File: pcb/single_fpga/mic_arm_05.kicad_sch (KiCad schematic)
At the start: 18 parts, among them U104 CDCLVC1108PW, U41 IM72D128V01XTMA1, U42 IM72D128V01XTMA1, U43 IM72D128V01XTMA1, U44 IM72D128V01XTMA1, U45 IM72D128V01XTMA1, U46 IM72D128V01XTMA1, U47 IM72D128V01XTMA1, U48 IM72D128V01XTMA1

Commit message: Fixed symbol library references.
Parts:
- U104: footprint PW0016A_N -> CDCLVC1108:PW0016A_N
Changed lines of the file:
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@@
 			)
 		)
-		(property "Footprint" "PW0016A_N"
+		(property "Footprint" "CDCLVC1108:PW0016A_N"
 			(at 229.87 95.25 0)
 			(hide yes)

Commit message: Fixed footprints. Added missing mic. Relinked placed footprints.
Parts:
- U41, U42, U43, U44, U45, U46, U47, U48: footprint (none) -> IM72D128:IFX-PG-LLGA-5-4
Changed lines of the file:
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@@
 			)
 		)
-		(property "Footprint" ""
+		(property "Footprint" "IM72D128:IFX-PG-LLGA-5-4"
 			(at 59.69 160.02 0)
 			(hide yes)
@@
 			)
 		)
-		(property "Footprint" ""
+		(property "Footprint" "IM72D128:IFX-PG-LLGA-5-4"
 			(at 135.89 160.02 0)
 			(hide yes)
@@
 			)
 		)
-		(property "Footprint" ""
+		(property "Footprint" "IM72D128:IFX-PG-LLGA-5-4"
 			(at 59.69 83.82 0)
 			(hide yes)
@@
 			)
 		)
-		(property "Footprint" ""
+		(property "Footprint" "IM72D128:IFX-PG-LLGA-5-4"
 			(at 59.69 120.65 0)
 			(hide yes)
@@
 			)
 		)
-		(property "Footprint" ""
+		(property "Footprint" "IM72D128:IFX-PG-LLGA-5-4"
 			(at 59.69 44.45 0)
 			(hide yes)
@@
 			)
 		)
-		(property "Footprint" ""
+		(property "Footprint" "IM72D128:IFX-PG-LLGA-5-4"
 			(at 135.89 83.82 0)
 			(hide yes)
@@
 			)
 		)
-		(property "Footprint" ""
+		(property "Footprint" "IM72D128:IFX-PG-LLGA-5-4"
 			(at 135.89 44.45 0)
 			(hide yes)
@@
 			)
 		)
-		(property "Footprint" ""
+		(property "Footprint" "IM72D128:IFX-PG-LLGA-5-4"
 			(at 135.89 120.65 0)
 			(hide yes)

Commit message: Updated all refdes's.
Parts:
- removed C58, C59, C60, C61, C62, C63, C64, C65: 100nF, Capacitor_SMD:C_0603_1608Metric, symbol Device:C
- removed R10: 10k, PCM_SparkFun-Resistor:R_0603_1608Metric, symbol PCM_SparkFun-Resistor:10k_0603
- removed U104: CDCLVC1108PW, CDCLVC1108:PW0016A_N, symbol CDCLVC1108:CDCLVC1108PW
- removed U41, U42, U43, U44, U45: IM72D128V01XTMA1, IM72D128:IFX-PG-LLGA-5-4, symbol multi_fpga:IM72D128
- added C41, C42, C43, C44, C45, C46, C47, C48: 100nF, Capacitor_SMD:C_0603_1608Metric, symbol Device:C
- added R6: 10k, PCM_SparkFun-Resistor:R_0603_1608Metric, symbol PCM_SparkFun-Resistor:10k_0603
- added U49, U50, U51, U52, U53: IM72D128V01XTMA1, IM72D128:IFX-PG-LLGA-5-4, symbol multi_fpga:IM72D128
- added U54: CDCLVC1108PW, CDCLVC1108:PW0016A_N, symbol CDCLVC1108:CDCLVC1108PW
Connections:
- net ARM_05_CLK: now also U54.1 (CLKIN)
- net CLK_3V3: now also R6.2, U54.10 (VDD), U54.14 (VDD), U54.5 (VDD)
- net DATA_20: now also U46.1 (DATA), U47.1 (DATA)
- net DATA_21: now also U48.1 (DATA), U49.1 (DATA)
- net DATA_22: now also U50.1 (DATA), U51.1 (DATA); no longer U46.1 (DATA)
- net DATA_23: now also U52.1 (DATA), U53.1 (DATA); no longer U47.1 (DATA), U48.1 (DATA)
- net GND: now also U46.4 (SEL), U48.4 (SEL), C41.2, C42.2, C43.2, C44.2, C45.2, C46.2, C47.2, C48.2, U49.5 (GND), U50.4 (SEL), U50.5 (GND), U51.5 (GND), U52.4 (SEL), U52.5 (GND), U53.5 (GND), U54.12 (GND), U54.4 (GND), U54.7 (GND); no longer U47.4 (SEL)
- net MIC_3V3: now also U47.4 (SEL), C41.1, C42.1, C43.1, C44.1, C45.1, C46.1, C47.1, C48.1, U49.2 (VDD), U49.4 (SEL), U50.2 (VDD), U51.2 (VDD), U51.4 (SEL), U52.2 (VDD), U53.2 (VDD), U53.4 (SEL); no longer U46.4 (SEL), U48.4 (SEL)
- net MIC_CLK_40: now also U46.3 (CLK), U54.3 (Y0)
- net MIC_CLK_41: now also U47.3 (CLK), U54.16 (Y1)
- net MIC_CLK_42: now also U48.3 (CLK), U54.13 (Y2)
- net MIC_CLK_43: now also U49.3 (CLK), U54.15 (Y3)
- net MIC_CLK_44: now also U50.3 (CLK), U54.6 (Y4)
- net MIC_CLK_45: now also U51.3 (CLK), U54.11 (Y5); no longer U46.3 (CLK)
- net MIC_CLK_46: now also U52.3 (CLK), U54.8 (Y6); no longer U47.3 (CLK)
- net MIC_CLK_47: now also U53.3 (CLK), U54.9 (Y7); no longer U48.3 (CLK)
- new net: R6.1, U54.2 (1G)

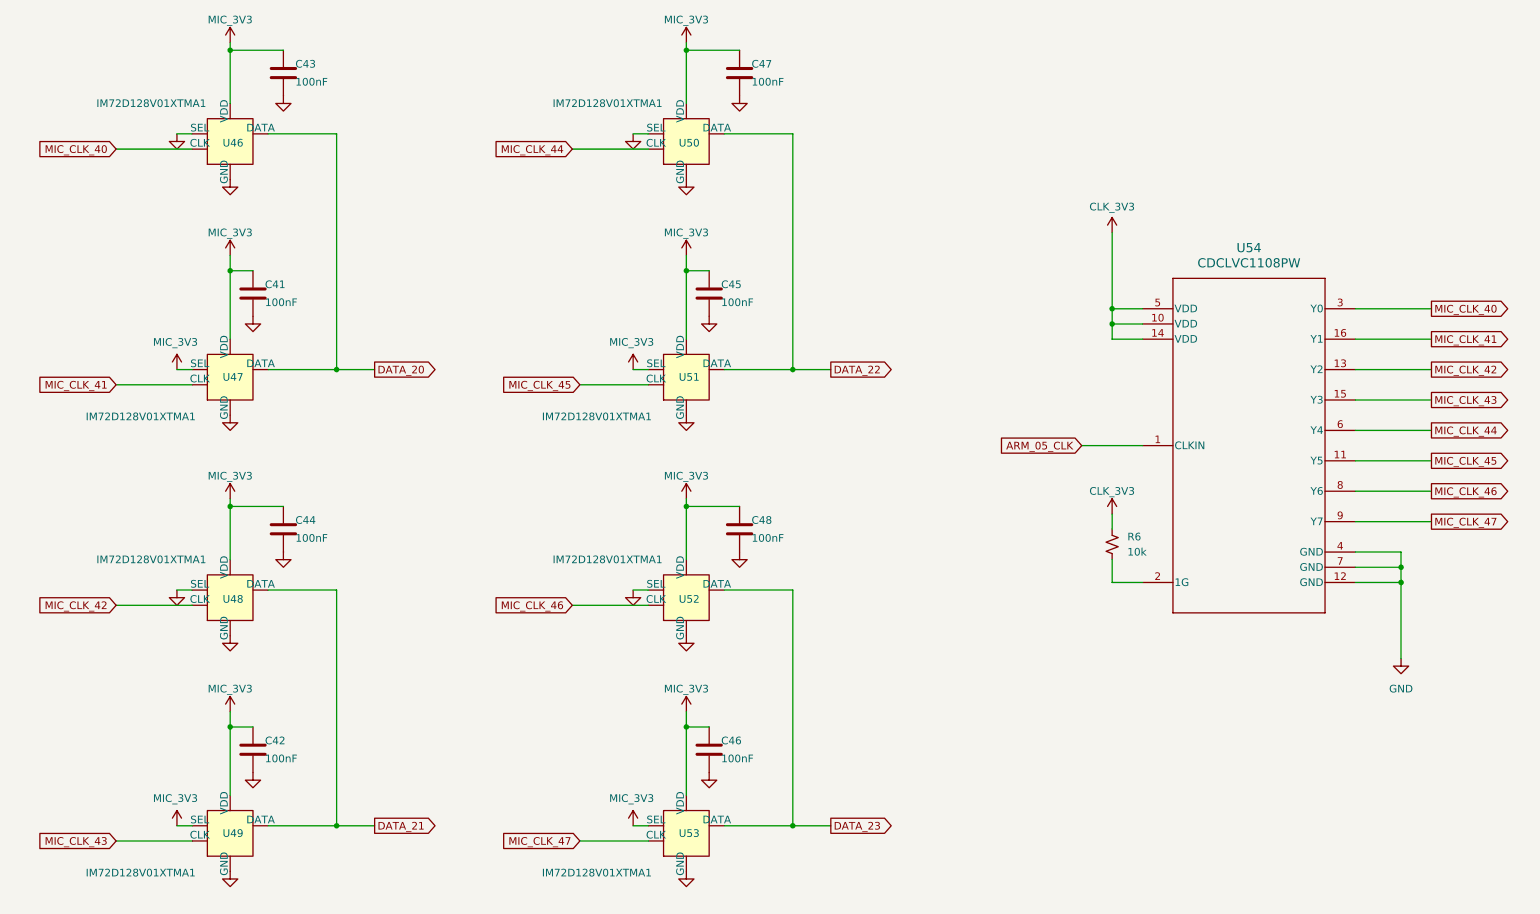
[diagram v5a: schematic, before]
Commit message: Changed mic symbol to improve readability.
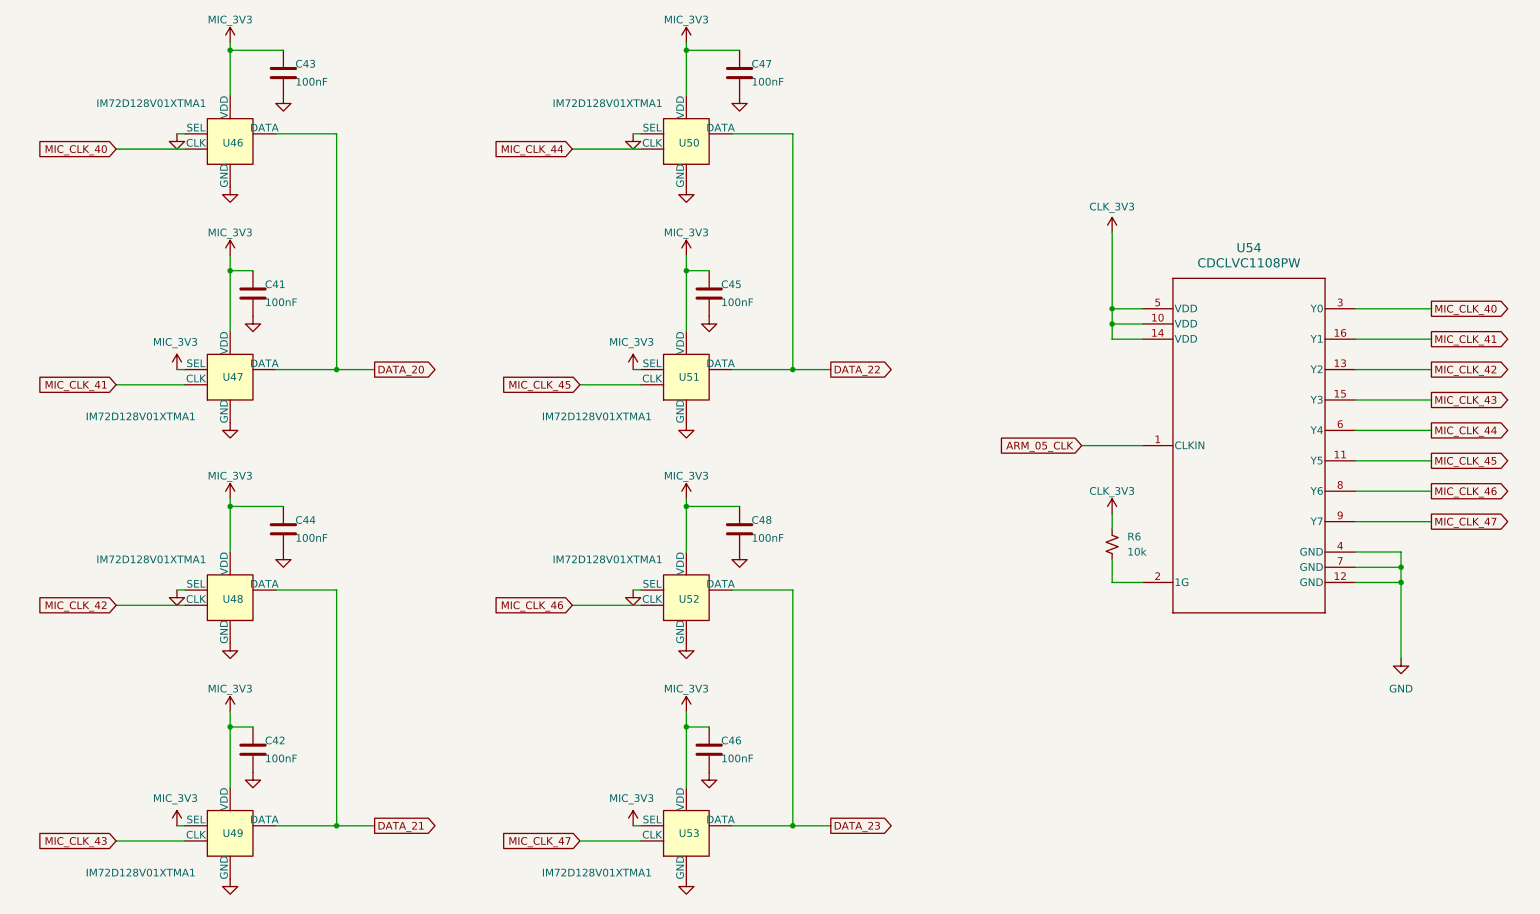
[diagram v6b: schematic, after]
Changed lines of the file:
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@@
 	(wire
 		(pts
-			(xy 153.67 119.38) (xy 142.24 119.38)
+			(xy 153.67 119.38) (xy 143.51 119.38)
 		)
 		(stroke
@@
 	(wire
 		(pts
-			(xy 135.89 142.24) (xy 135.89 153.67)
+			(xy 135.89 142.24) (xy 135.89 152.4)
 		)
 		(stroke
@@
 	(wire
 		(pts
-			(xy 153.67 43.18) (xy 142.24 43.18)
+			(xy 153.67 43.18) (xy 143.51 43.18)
 		)
 		(stroke
@@
 	(wire
 		(pts
-			(xy 118.11 85.09) (xy 129.54 85.09)
+			(xy 118.11 85.09) (xy 128.27 85.09)
 		)
 		(stroke
@@
 	(wire
 		(pts
-			(xy 127 43.18) (xy 129.54 43.18)
+			(xy 127 43.18) (xy 128.27 43.18)
 		)
 		(stroke
@@
 	(wire
 		(pts
-			(xy 50.8 43.18) (xy 53.34 43.18)
+			(xy 50.8 43.18) (xy 52.07 43.18)
 		)
 		(stroke
@@
 	(wire
 		(pts
-			(xy 142.24 82.55) (xy 153.67 82.55)
+			(xy 143.51 82.55) (xy 153.67 82.55)
 		)
 		(stroke
@@
 	(wire
 		(pts
-			(xy 40.64 45.72) (xy 53.34 45.72)
+			(xy 40.64 45.72) (xy 52.07 45.72)
 		)
 		(stroke
@@
 	(wire
 		(pts
-			(xy 50.8 82.55) (xy 53.34 82.55)
+			(xy 50.8 82.55) (xy 52.07 82.55)
 		)
 		(stroke
@@
 	(wire
 		(pts
-			(xy 59.69 66.04) (xy 59.69 77.47)
+			(xy 59.69 66.04) (xy 59.69 76.2)
 		)
 		(stroke
@@
 	(wire
 		(pts
-			(xy 135.89 105.41) (xy 135.89 114.3)
+			(xy 135.89 105.41) (xy 135.89 113.03)
 		)
 		(stroke
@@
 	(wire
 		(pts
-			(xy 59.69 29.21) (xy 59.69 38.1)
+			(xy 59.69 29.21) (xy 59.69 36.83)
 		)
 		(stroke
@@
 	(wire
 		(pts
-			(xy 66.04 82.55) (xy 77.47 82.55)
+			(xy 67.31 82.55) (xy 77.47 82.55)
 		)
 		(stroke
@@
 	(wire
 		(pts
-			(xy 59.69 105.41) (xy 59.69 114.3)
+			(xy 59.69 105.41) (xy 59.69 113.03)
 		)
 		(stroke
@@
 	(wire
 		(pts
-			(xy 40.64 161.29) (xy 53.34 161.29)
+			(xy 40.64 161.29) (xy 52.07 161.29)
 		)
 		(stroke
@@
 	(wire
 		(pts
-			(xy 127 119.38) (xy 129.54 119.38)
+			(xy 127 119.38) (xy 128.27 119.38)
 		)
 		(stroke
@@
 	(wire
 		(pts
-			(xy 50.8 158.75) (xy 53.34 158.75)
+			(xy 50.8 158.75) (xy 52.07 158.75)
 		)
 		(stroke
@@
 	(wire
 		(pts
-			(xy 50.8 119.38) (xy 53.34 119.38)
+			(xy 50.8 119.38) (xy 52.07 119.38)
 		)
 		(stroke
@@
 	(wire
 		(pts
-			(xy 40.64 121.92) (xy 53.34 121.92)
+			(xy 40.64 121.92) (xy 52.07 121.92)
 		)
 		(stroke
@@
 	(wire
 		(pts
-			(xy 77.47 119.38) (xy 66.04 119.38)
+			(xy 77.47 119.38) (xy 67.31 119.38)
 		)
 		(stroke
@@
 	(wire
 		(pts
-			(xy 118.11 161.29) (xy 129.54 161.29)
+			(xy 118.11 161.29) (xy 128.27 161.29)
 		)
 		(stroke
@@
 	(wire
 		(pts
-			(xy 116.84 45.72) (xy 129.54 45.72)
+			(xy 116.84 45.72) (xy 128.27 45.72)
 		)
 		(stroke
@@
 	(wire
 		(pts
-			(xy 135.89 66.04) (xy 135.89 77.47)
+			(xy 135.89 66.04) (xy 135.89 76.2)
 		)
 		(stroke
@@
 	(wire
 		(pts
-			(xy 135.89 29.21) (xy 135.89 38.1)
+			(xy 135.89 29.21) (xy 135.89 36.83)
 		)
 		(stroke
@@
 	(wire
 		(pts
-			(xy 66.04 158.75) (xy 77.47 158.75)
+			(xy 67.31 158.75) (xy 77.47 158.75)
 		)
 		(stroke
@@
 	(wire
 		(pts
-			(xy 142.24 158.75) (xy 153.67 158.75)
+			(xy 143.51 158.75) (xy 153.67 158.75)
 		)
 		(stroke
@@
 	(wire
 		(pts
-			(xy 127 82.55) (xy 129.54 82.55)
+			(xy 127 82.55) (xy 128.27 82.55)
 		)
 		(stroke
@@
 	(wire
 		(pts
-			(xy 77.47 43.18) (xy 66.04 43.18)
+			(xy 77.47 43.18) (xy 67.31 43.18)
 		)
 		(stroke
@@
 	(wire
 		(pts
-			(xy 127 158.75) (xy 129.54 158.75)
+			(xy 127 158.75) (xy 128.27 158.75)
 		)
 		(stroke
@@
 	(wire
 		(pts
-			(xy 40.64 85.09) (xy 53.34 85.09)
+			(xy 40.64 85.09) (xy 52.07 85.09)
 		)
 		(stroke
@@
 	(wire
 		(pts
-			(xy 116.84 121.92) (xy 129.54 121.92)
+			(xy 116.84 121.92) (xy 128.27 121.92)
 		)
 		(stroke
@@
 	(wire
 		(pts
-			(xy 59.69 142.24) (xy 59.69 153.67)
+			(xy 59.69 142.24) (xy 59.69 152.4)
 		)
 		(stroke
@@
 	(symbol
 		(lib_id "power:GND")
-		(at 135.89 50.8 0)
+		(at 135.89 52.07 0)
 		(unit 1)
 		(body_style 1)
@@
 	(symbol
 		(lib_id "power:GND")
-		(at 135.89 166.37 0)
+		(at 135.89 167.64 0)
 		(unit 1)
 		(body_style 1)
@@
 	(symbol
 		(lib_id "power:GND")
-		(at 135.89 90.17 0)
+		(at 135.89 91.44 0)
 		(unit 1)
 		(body_style 1)
@@
 	(symbol
 		(lib_id "power:GND")
-		(at 59.69 90.17 0)
+		(at 59.69 91.44 0)
 		(unit 1)
 		(body_style 1)
@@
 	(symbol
 		(lib_id "power:GND")
-		(at 59.69 166.37 0)
+		(at 59.69 167.64 0)
 		(unit 1)
 		(body_style 1)
@@
 	(symbol
 		(lib_id "power:GND")
-		(at 59.69 127 0)
+		(at 59.69 128.27 0)
 		(unit 1)
 		(body_style 1)
@@
 	(symbol
 		(lib_id "power:GND")
-		(at 59.69 50.8 0)
+		(at 59.69 52.07 0)
 		(unit 1)
 		(body_style 1)
@@
 	(symbol
 		(lib_id "power:GND")
-		(at 135.89 127 0)
+		(at 135.89 128.27 0)
 		(unit 1)
 		(body_style 1)

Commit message: Used new mic symbol and cleaned up.
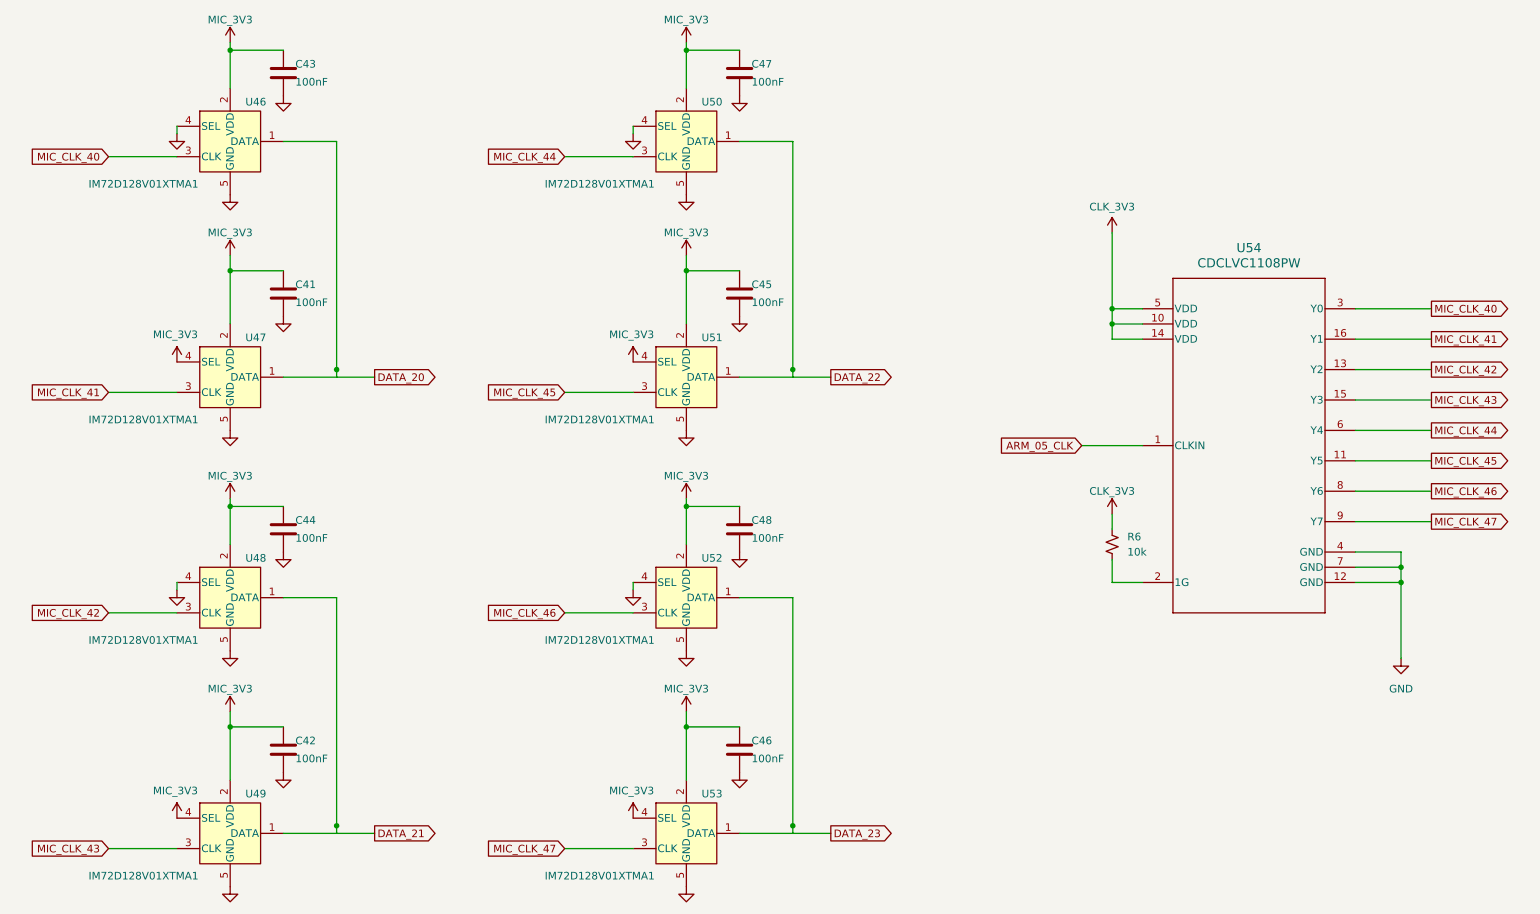
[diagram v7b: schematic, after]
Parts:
- U46, U47, U48, U49, U50, U51, U52, U53: footprint IM72D128:IFX-PG-LLGA-5-4 -> (none)
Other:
- moved on the sheet: C41, C42, C45, C46
